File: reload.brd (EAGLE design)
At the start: 44 x 31 mm, 24 parts, among them IC1 MCP6002, IC2 TS 1117, Q1 IRLZ34N, X1 MKDSN1,5/3-5,08

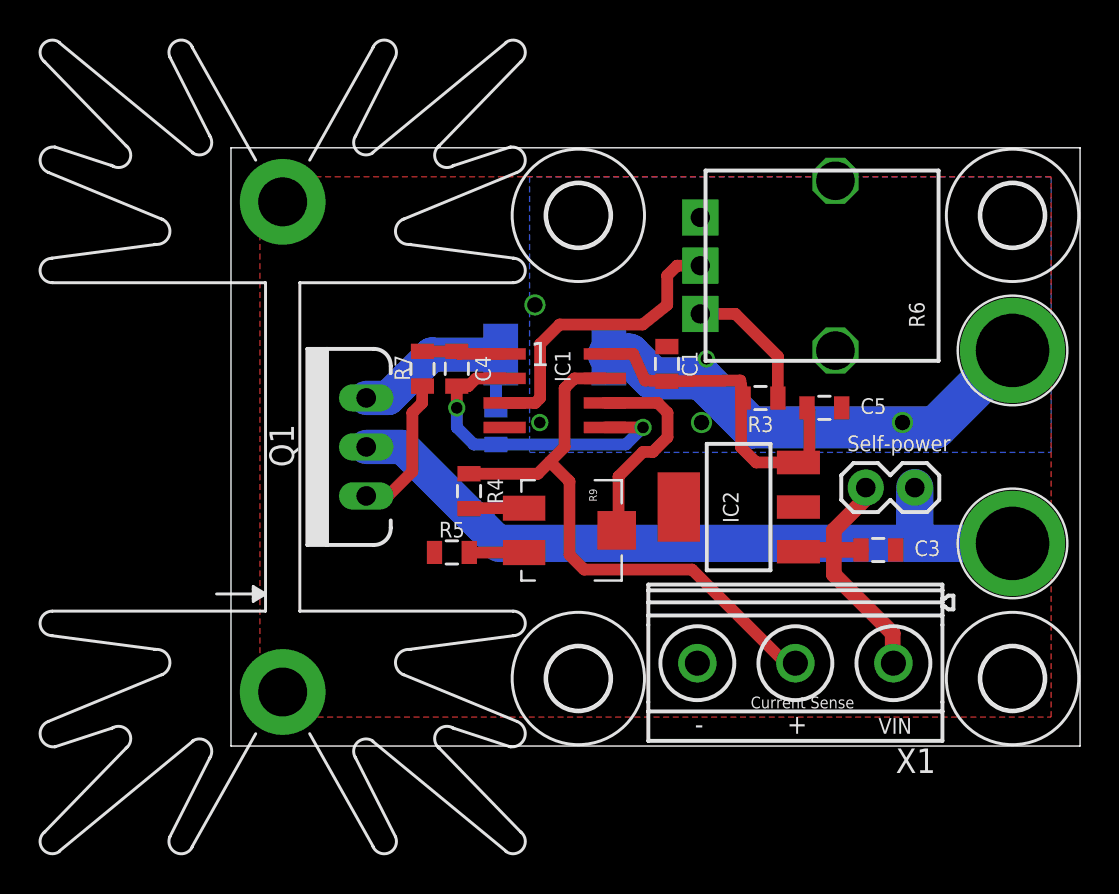
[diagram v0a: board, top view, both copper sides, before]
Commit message: Delete heatsink for panelize
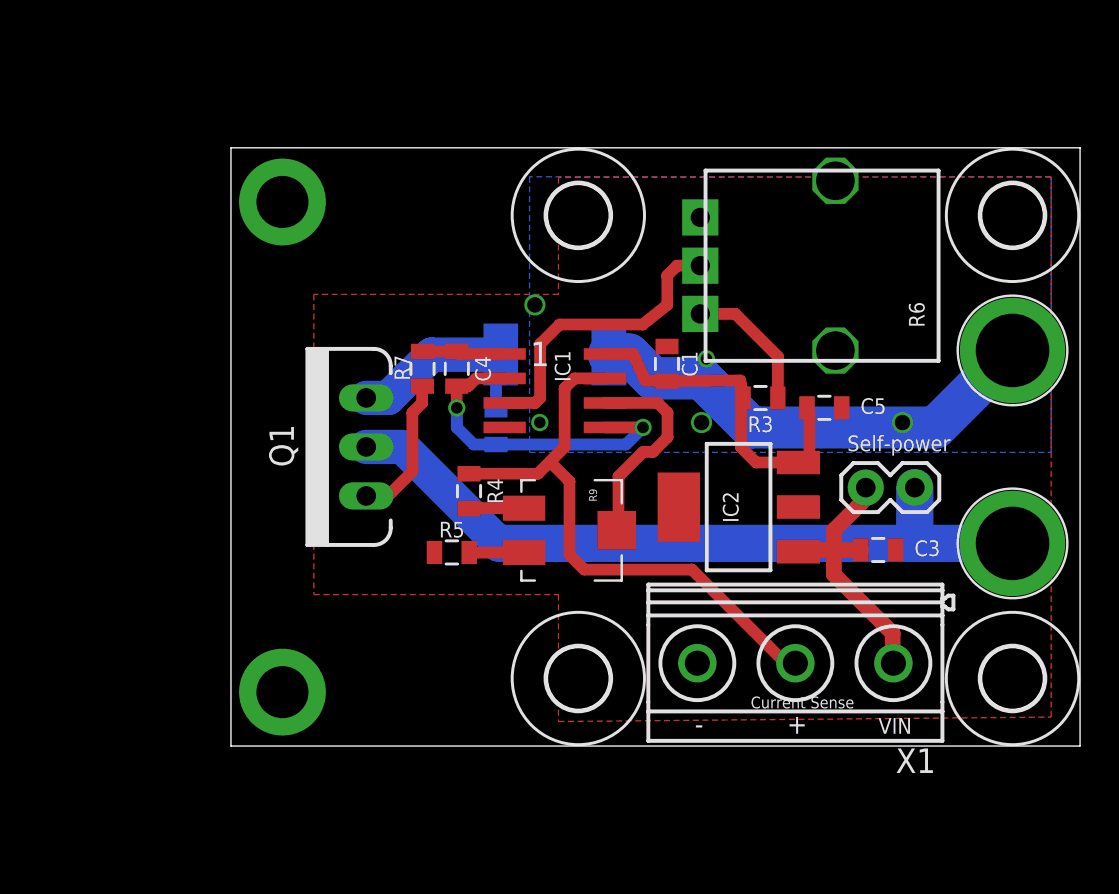
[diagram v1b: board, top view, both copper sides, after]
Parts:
- removed KK1: SK129-PAD, nickparts:SK129
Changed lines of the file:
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@@
 <setting verticaltext="up"/>
 </settings>
-<grid distance="1.27" unitdist="mm" unit="mm" style="lines" multiple="1" display="yes" altdistance="10" altunitdist="mil" altunit="mil"/>
+<grid distance="1.27" unitdist="mm" unit="mm" style="lines" multiple="1" display="yes" altdistance="5" altunitdist="mil" altunit="mil"/>
 <layers>
 <layer number="1" name="Top" color="4" fill="1" visible="yes" active="yes"/>
@@
 <layer number="37" name="tTest" color="7" fill="1" visible="no" active="yes"/>
 <layer number="38" name="bTest" color="7" fill="1" visible="no" active="yes"/>
-<layer number="39" name="tKeepout" color="4" fill="11" visible="no" active="yes"/>
+<layer number="39" name="tKeepout" color="4" fill="11" visible="yes" active="yes"/>
 <layer number="40" name="bKeepout" color="1" fill="11" visible="no" active="yes"/>
-<layer number="41" name="tRestrict" color="4" fill="10" visible="no" active="yes"/>
+<layer number="41" name="tRestrict" color="4" fill="10" visible="yes" active="yes"/>
 <layer number="42" name="bRestrict" color="1" fill="10" visible="no" active="yes"/>
 <layer number="43" name="vRestrict" color="2" fill="10" visible="no" active="yes"/>
@@
 <attribute name="NAME" x="36.084" y="9.8425" size="0.8128" layer="25" align="bottom-center"/>
 </element>
-<element name="KK1" library="nickparts" package="SK129" value="SK129-PAD" x="1.79" y="15.5" smashed="yes" rot="R90"/>
 <element name="R7" library="SparkFun-Passives" package="0805" value="100" x="9.922" y="19.55" smashed="yes" rot="R90">
 <attribute name="NAME" x="9.287" y="19.6025" size="0.8128" layer="25" font="vector" rot="R90" align="bottom-center"/>
@@
 <contactref element="IC2" pad="2"/>
 <polygon width="0.8128" layer="1">
-<vertex x="1.5" y="1.5"/>
+<vertex x="4.294" y="7.85"/>
+<vertex x="16.97" y="7.85"/>
+<vertex x="16.97" y="1.27"/>
 <vertex x="42.5" y="1.5"/>
 <vertex x="42.5" y="29.5"/>
-<vertex x="1.5" y="29.5"/>
+<vertex x="16.97" y="29.464"/>
+<vertex x="16.97" y="23.404"/>
+<vertex x="4.294" y="23.404"/>
 </polygon>
 <contactref element="C5" pad="2"/>
@@
 <wire x1="28.34" y1="20.19" x2="28.34" y2="18.034" width="0.6096" layer="1"/>
 </signal>
+<signal name="N$8">
+<via x="2.667" y="28.194" extent="1-16" drill="2.7" diameter="4.5"/>
+</signal>
+<signal name="N$10">
+<via x="2.667" y="2.794" extent="1-16" drill="2.7" diameter="4.5"/>
+</signal>
 </signals>

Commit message: rearrange part identifiers for silkscreen change bottom ground plane
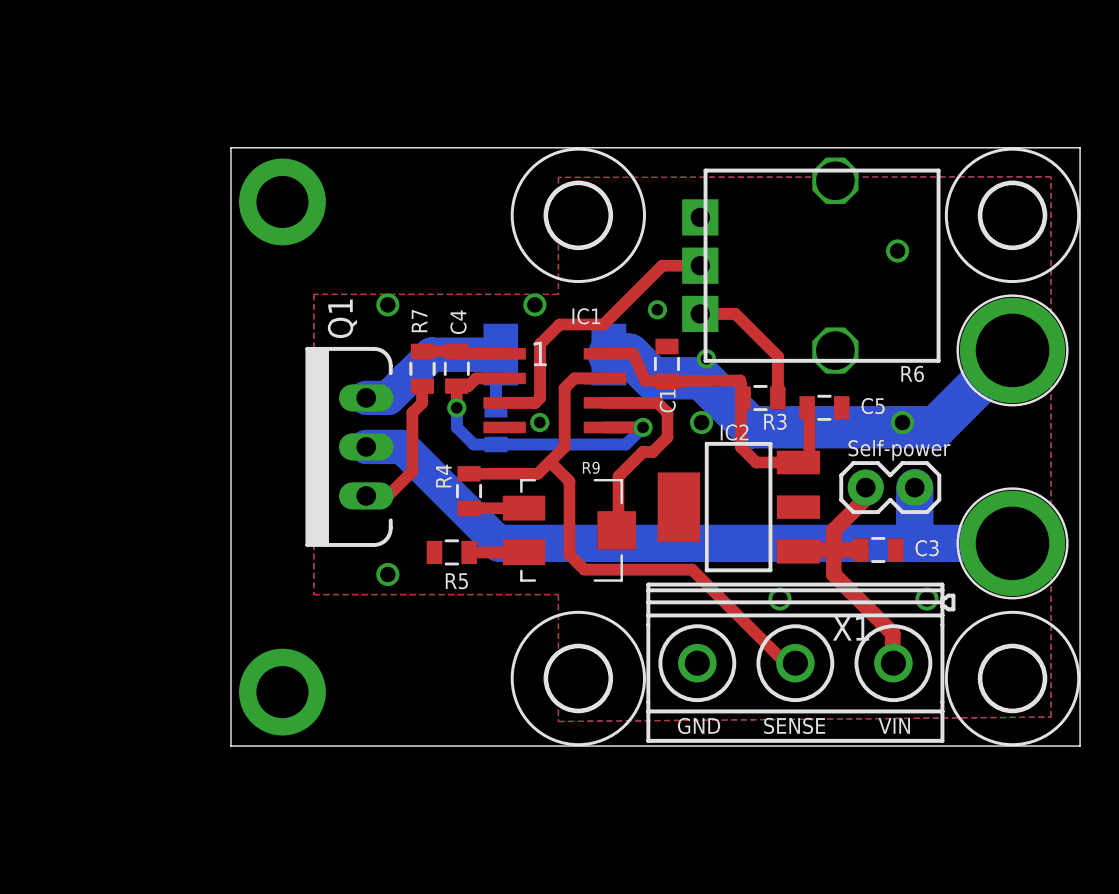
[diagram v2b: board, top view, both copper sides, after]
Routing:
- net N$4: track 15.6 -> 14.7 mm
- net GND: vias 5 -> 11
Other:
- board text added: "GND"
- board text added: "SENSE"
- board text removed: "+"
- board text removed: "-"
- board text removed: "Current Sense"

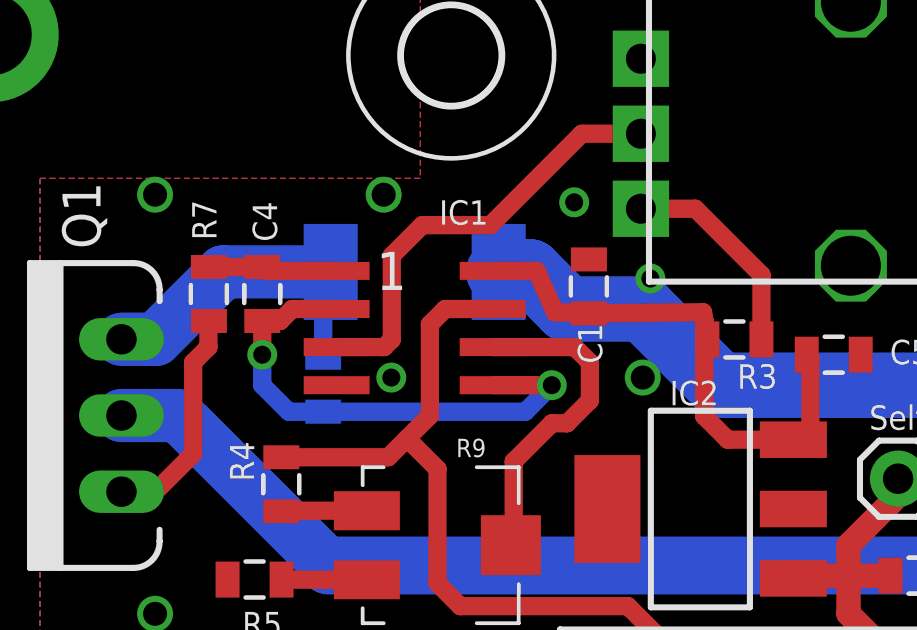
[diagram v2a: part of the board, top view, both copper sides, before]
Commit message: improve for production
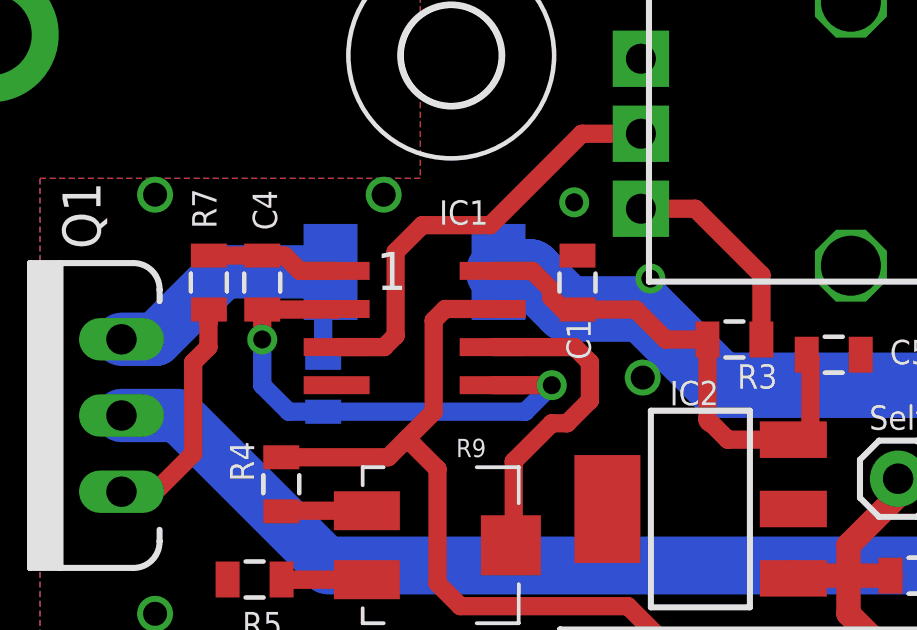
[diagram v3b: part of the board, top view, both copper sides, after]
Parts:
- moved C1 0.40 mm to (22.2, 19.9)
- moved C4 0.38 mm to (11.7, 19.9)
- moved R7 0.38 mm to (9.92, 19.9)
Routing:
- net VCC: track 19.4 -> 17.5 mm
- net GND: vias 11 -> 10
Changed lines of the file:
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@@
 <?xml version="1.0" encoding="utf-8"?>
 <!DOCTYPE eagle SYSTEM "eagle.dtd">
-<eagle version="6.6.0">
+<eagle version="7.4.0">
 <drawing>
 <settings>
@@
 <pass name="Default">
 <param name="RoutingGrid" value="50mil"/>
+<param name="AutoGrid" value="1"/>
+<param name="Efforts" value="0"/>
+<param name="TopRouterVariant" value="1"/>
 <param name="tpViaShape" value="round"/>
 <param name="PrefDir.1" value="|"/>
@@
 <attribute name="NAME" x="28.202" y="17.2085" size="0.8128" layer="25" font="vector" rot="R180" align="bottom-center"/>
 </element>
-<element name="C1" library="SparkFun-Passives" package="0805" value="0.1u" x="22.59" y="19.804" smashed="yes" rot="R90">
-<attribute name="NAME" x="23.0345" y="17.899" size="0.8128" layer="25" rot="R90" align="bottom-center"/>
+<element name="C1" library="SparkFun-Passives" package="0805" value="0.1u" x="22.209" y="19.931" smashed="yes" rot="R90">
+<attribute name="NAME" x="22.6535" y="18.026" size="0.8128" layer="25" rot="R90" align="bottom-center"/>
 </element>
 <element name="R5" library="SparkFun-Passives" package="0805" value="10k 1%" x="11.446" y="10.033" smashed="yes" rot="R180">
@@
 <attribute name="NAME" x="36.084" y="9.8425" size="0.8128" layer="25" align="bottom-center"/>
 </element>
-<element name="R7" library="SparkFun-Passives" package="0805" value="100" x="9.922" y="19.55" smashed="yes" rot="R90">
-<attribute name="NAME" x="10.176" y="22.0155" size="0.8128" layer="25" font="vector" rot="R90" align="bottom-center"/>
+<element name="R7" library="SparkFun-Passives" package="0805" value="100" x="9.922" y="19.931" smashed="yes" rot="R90">
+<attribute name="NAME" x="10.176" y="22.3965" size="0.8128" layer="25" font="vector" rot="R90" align="bottom-center"/>
 </element>
 <element name="IC1" library="nickparts" package="SOP08" value="MCP6002" x="16.78" y="18.415" smashed="yes" rot="R270">
@@
 <attribute name="NAME" x="12.3985" y="15.7955" size="0.8128" layer="26" rot="MR270" align="bottom-center"/>
 </element>
-<element name="C4" library="SparkFun-Passives" package="0805" value="0.1u" x="11.7" y="19.55" smashed="yes" rot="R270">
-<attribute name="NAME" x="11.3825" y="21.963" size="0.8128" layer="25" rot="R270" align="bottom-center"/>
+<element name="C4" library="SparkFun-Passives" package="0805" value="0.1u" x="11.7" y="19.931" smashed="yes" rot="R270">
+<attribute name="NAME" x="11.3825" y="22.344" size="0.8128" layer="25" rot="R270" align="bottom-center"/>
 </element>
 <element name="JP2" library="SparkFun-Passives" package="1X02" value="" x="32.895" y="13.3925" smashed="yes">
@@
 <contactref element="IC1" pad="2"/>
 <contactref element="C4" pad="2"/>
-<via x="11.7" y="17.526" extent="1-16" drill="0.6"/>
-<wire x1="11.7" y1="17.526" x2="11.7" y2="18.65" width="0.6096" layer="1"/>
+<via x="11.7" y="18.034" extent="1-16" drill="0.6"/>
+<wire x1="11.7" y1="18.034" x2="11.7" y2="19.031" width="0.6096" layer="1"/>
 <wire x1="13.732" y1="15.62575" x2="12.58425" y2="15.62575" width="0.6096" layer="16"/>
 <wire x1="12.58425" y1="15.62575" x2="11.7" y2="16.51" width="0.6096" layer="16"/>
-<wire x1="11.7" y1="16.51" x2="11.7" y2="17.526" width="0.6096" layer="16"/>
+<wire x1="11.7" y1="16.51" x2="11.7" y2="18.034" width="0.6096" layer="16"/>
 <wire x1="19.38" y1="16.51" x2="21.352" y2="16.51" width="0.6096" layer="1"/>
 <via x="21.352" y="16.51" extent="1-16" drill="0.6"/>
 <wire x1="21.352" y1="16.51" x2="20.46775" y2="15.62575" width="0.6096" layer="16"/>
 <wire x1="20.46775" y1="15.62575" x2="13.732" y2="15.62575" width="0.6096" layer="16"/>
-<wire x1="14.18" y1="19.05" x2="12.7" y2="19.05" width="0.6096" layer="1"/>
-<wire x1="12.7" y1="19.05" x2="12.3" y2="18.65" width="0.6096" layer="1"/>
-<wire x1="12.3" y1="18.65" x2="11.7" y2="18.65" width="0.6096" layer="1"/>
+<wire x1="14.18" y1="19.05" x2="14.161" y2="19.031" width="0.6096" layer="1"/>
+<wire x1="14.161" y1="19.031" x2="11.7" y2="19.031" width="0.6096" layer="1"/>
 </signal>
 <signal name="GND">
@@
 <contactref element="IC1" pad="4"/>
 <contactref element="IC2" pad="2"/>
-<polygon width="0.8128" layer="1" isolate="0.254">
+<polygon width="0.8128" layer="1" isolate="0.6096">
 <vertex x="4.294" y="7.85"/>
 <vertex x="16.97" y="7.85"/>
@@
 <wire x1="26.94" y1="16.51" x2="36.51" y2="16.51" width="2.1844" layer="16"/>
 <wire x1="36.51" y1="16.51" x2="40.5" y2="20.5" width="2.1844" layer="16"/>
-<via x="16.002" y="16.764" extent="1-16" drill="0.6"/>
 <via x="24.638" y="20.066" extent="1-16" drill="0.6"/>
 <via x="24.384" y="16.764" extent="1-16" drill="0.8"/>
 <via x="15.748" y="22.86" extent="1-16" drill="0.8"/>
 <via x="34.798" y="16.764" extent="1-16" drill="0.8"/>
-<polygon width="0.8128" layer="16" isolate="0.254">
+<polygon width="0.8128" layer="16" isolate="0.6096">
 <vertex x="4.294" y="7.85"/>
 <vertex x="16.97" y="7.85"/>
@@
 <contactref element="IC1" pad="3"/>
 <wire x1="14.18" y1="17.78" x2="15.764" y2="17.78" width="0.6096" layer="1"/>
-<wire x1="15.764" y1="17.78" x2="16.018" y2="18.034" width="0.6096" layer="1"/>
-<wire x1="16.018" y1="18.034" x2="16.018" y2="20.828" width="0.6096" layer="1"/>
+<wire x1="15.764" y1="17.78" x2="16.145" y2="18.161" width="0.6096" layer="1"/>
+<wire x1="16.145" y1="18.161" x2="16.145" y2="20.955" width="0.6096" layer="1"/>
 <wire x1="24.3215" y1="24.892" x2="22.352" y2="24.892" width="0.6096" layer="1"/>
-<wire x1="17.034" y1="21.844" x2="16.018" y2="20.828" width="0.6096" layer="1"/>
+<wire x1="17.034" y1="21.844" x2="16.145" y2="20.955" width="0.6096" layer="1"/>
 <wire x1="22.352" y1="24.892" x2="19.304" y2="21.844" width="0.6096" layer="1"/>
 <wire x1="19.304" y1="21.844" x2="17.034" y2="21.844" width="0.6096" layer="1"/>
@@
 <contactref element="IC1" pad="7"/>
 <contactref element="X1" pad="2"/>
-<wire x1="17.288" y1="15.494" x2="17.288" y2="18.542" width="0.6096" layer="1"/>
-<wire x1="17.288" y1="18.542" x2="17.796" y2="19.05" width="0.6096" layer="1"/>
+<wire x1="17.415" y1="15.621" x2="17.415" y2="18.669" width="0.6096" layer="1"/>
+<wire x1="17.415" y1="18.669" x2="17.796" y2="19.05" width="0.6096" layer="1"/>
 <wire x1="17.796" y1="19.05" x2="19.38" y2="19.05" width="0.6096" layer="1"/>
 <wire x1="12.335" y1="14.108" x2="15.902" y2="14.108" width="0.6096" layer="1"/>
 <wire x1="15.902" y1="14.108" x2="16.526" y2="14.732" width="0.6096" layer="1"/>
-<wire x1="16.526" y1="14.732" x2="17.288" y2="15.494" width="0.6096" layer="1"/>
+<wire x1="16.526" y1="14.732" x2="17.415" y2="15.621" width="0.6096" layer="1"/>
 <wire x1="18.304" y1="9.144" x2="17.542" y2="9.906" width="0.6096" layer="1"/>
 <wire x1="17.542" y1="9.906" x2="17.542" y2="13.716" width="0.6096" layer="1"/>
@@
 <contactref element="IC1" pad="1"/>
 <contactref element="C4" pad="1"/>
-<wire x1="14.18" y1="20.32" x2="11.83" y2="20.32" width="0.6096" layer="1"/>
-<wire x1="11.83" y1="20.32" x2="11.7" y2="20.45" width="0.6096" layer="1" curve="-90"/>
-<wire x1="11.7" y1="20.45" x2="9.922" y2="20.45" width="0.6096" layer="1"/>
+<wire x1="11.7" y1="20.831" x2="9.922" y2="20.831" width="0.6096" layer="1"/>
+<wire x1="14.18" y1="20.32" x2="12.954" y2="20.32" width="0.6096" layer="1"/>
+<wire x1="12.954" y1="20.32" x2="12.443" y2="20.831" width="0.6096" layer="1"/>
+<wire x1="12.443" y1="20.831" x2="11.7" y2="20.831" width="0.6096" layer="1"/>
 </signal>
 <signal name="N$9">
 <contactref element="R7" pad="1"/>
 <contactref element="Q1" pad="1"/>
-<wire x1="9.922" y1="18.65" x2="9.906" y2="18.5895" width="0.6096" layer="1"/>
+<wire x1="9.922" y1="19.031" x2="9.906" y2="18.5895" width="0.6096" layer="1"/>
 <wire x1="9.906" y1="18.5895" x2="9.906" y2="17.78" width="0.6096" layer="1"/>
 <wire x1="9.906" y1="17.78" x2="9.398" y2="17.272" width="0.6096" layer="1"/>
@@
 <contactref element="IC2" pad="3"/>
 <contactref element="C5" pad="1"/>
-<wire x1="26.432" y1="18.688" x2="26.54" y2="18.034" width="0.6096" layer="1"/>
-<wire x1="26.54" y1="18.034" x2="26.394" y2="18.942" width="0.6096" layer="1"/>
-<wire x1="26.394" y1="18.942" x2="22.59" y2="18.904" width="0.6096" layer="1"/>
-<wire x1="22.59" y1="18.904" x2="21.46" y2="18.942" width="0.6096" layer="1"/>
-<wire x1="21.46" y1="18.942" x2="20.844" y2="20.32" width="0.6096" layer="1"/>
-<wire x1="20.844" y1="20.32" x2="19.38" y2="20.32" width="0.6096" layer="1"/>
 <wire x1="29.85" y1="17.526" x2="29.972" y2="17.404" width="0.6096" layer="1"/>
 <wire x1="29.972" y1="17.404" x2="29.972" y2="14.732" width="0.6096" layer="1"/>
 <wire x1="29.972" y1="14.732" x2="29.9339" y2="14.6939" width="0.6096" layer="1"/>
 <wire x1="29.9339" y1="14.6939" x2="29.4038" y2="14.6939" width="0.6096" layer="1"/>
-<wire x1="26.432" y1="18.688" x2="26.432" y2="15.478" width="0.6096" layer="1"/>
-<wire x1="26.432" y1="15.478" x2="27.2161" y2="14.6939" width="0.6096" layer="1"/>
+<wire x1="19.38" y1="20.32" x2="20.701" y2="20.32" width="0.6096" layer="1"/>
+<wire x1="20.701" y1="20.32" x2="21.336" y2="19.685" width="0.6096" layer="1"/>
+<wire x1="21.336" y1="19.685" x2="21.336" y2="19.431" width="0.6096" layer="1"/>
+<wire x1="21.336" y1="19.431" x2="21.736" y2="19.031" width="0.6096" layer="1"/>
+<wire x1="21.736" y1="19.031" x2="22.209" y2="19.031" width="0.6096" layer="1"/>
+<wire x1="22.209" y1="19.031" x2="24.149" y2="19.031" width="0.6096" layer="1"/>
+<wire x1="24.149" y1="19.031" x2="25.146" y2="18.034" width="0.6096" layer="1"/>
+<wire x1="25.146" y1="18.034" x2="26.54" y2="18.034" width="0.6096" layer="1"/>
+<wire x1="26.54" y1="18.034" x2="26.54" y2="15.37" width="0.6096" layer="1"/>
+<wire x1="26.54" y1="15.37" x2="26.67" y2="15.24" width="0.6096" layer="1" curve="90"/>
+<wire x1="26.67" y1="15.24" x2="27.2161" y2="14.6939" width="0.6096" layer="1"/>
 <wire x1="27.2161" y1="14.6939" x2="29.4038" y2="14.6939" width="0.6096" layer="1"/>
 </signal>
